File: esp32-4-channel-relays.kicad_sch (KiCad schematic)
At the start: 5 parts, among them U1 AMS1117-3.3

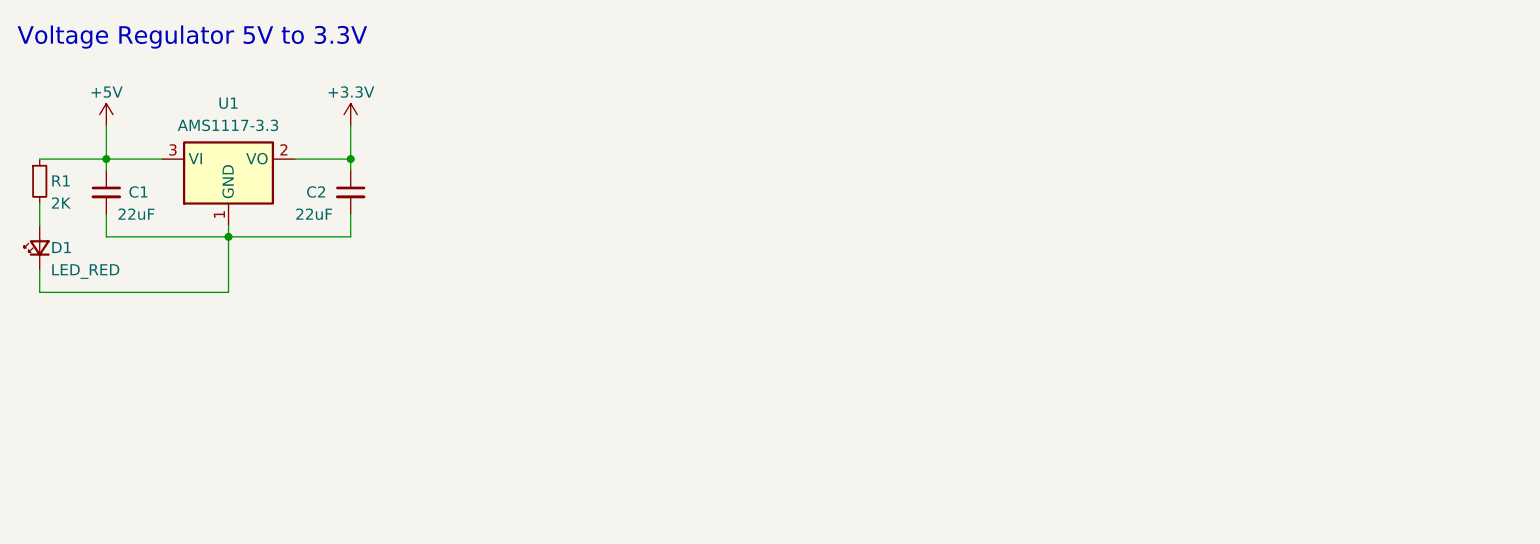
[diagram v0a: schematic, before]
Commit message: Add USB to serial converter
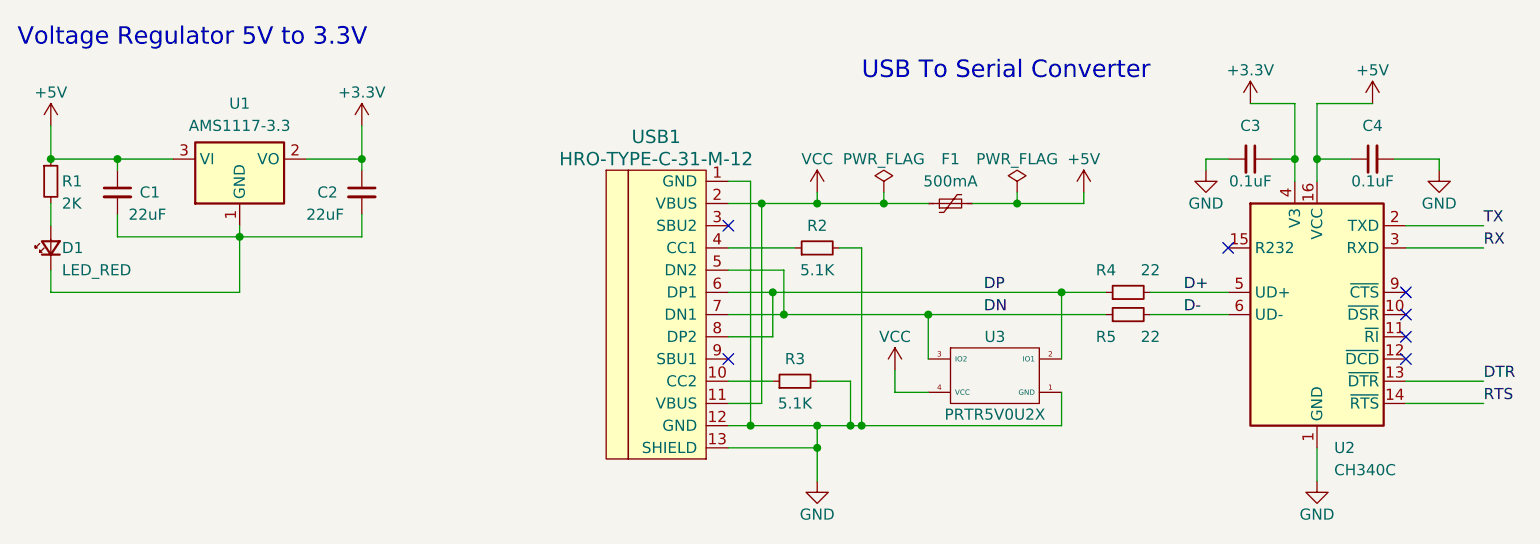
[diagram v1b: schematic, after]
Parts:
- added C3, C4: 0.1uF, symbol Device:C_Small
- added F1: 500mA, symbol Device:Polyfuse_Small
- added R2, R3: 5.1K, symbol Device:R_Small
- added R4, R5: 22, symbol Device:R_Small
- added U2: CH340C, Package_SO:SOIC-16_3.9x9.9mm_P1.27mm, symbol local_lib:CH340C
- added U3: PRTR5V0U2X, Package_TO_SOT_SMD:SOT-143, symbol local_lib:PRTR5V0U2X
- added USB1: HRO-TYPE-C-31-M-12, symbol local_lib:HRO-TYPE-C-31-M-12
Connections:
- net +3.3V: now also C3.1, U2.4 (V3)
- net +5V: now also C4.1, F1.2, U2.16 (VCC)
- new net: R3.1, USB1.10 (CC2)
- new net: R2.1, USB1.4 (CC1)
- new net D+: R4.2, U2.5 (UD+)
- new net D-: R5.2, U2.6 (UD-)
- new net DN: R5.1, U3.3 (IO2), USB1.5 (DN2), USB1.7 (DN1)
- new net DP: R4.1, U3.2 (IO1), USB1.6 (DP1), USB1.8 (DP2)
- new net DTR: U2.13 (~{DTR})
- new net GND: C3.2, C4.2, R2.2, R3.2, U2.1 (GND), U3.1 (GND), USB1.1 (GND), USB1.12 (GND), USB1.13 (SHIELD)
- new net RTS: U2.14 (~{RTS})
- new net RX: U2.3 (RXD)
- new net TX: U2.2 (TXD)
- new net VCC: F1.1, U3.4 (VCC), USB1.11 (VBUS), USB1.2 (VBUS)
- no-connect marks 0 -> 7
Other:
- note added: "USB To Serial Converter"
- moved on the sheet: C1, C2, D1, R1, U1

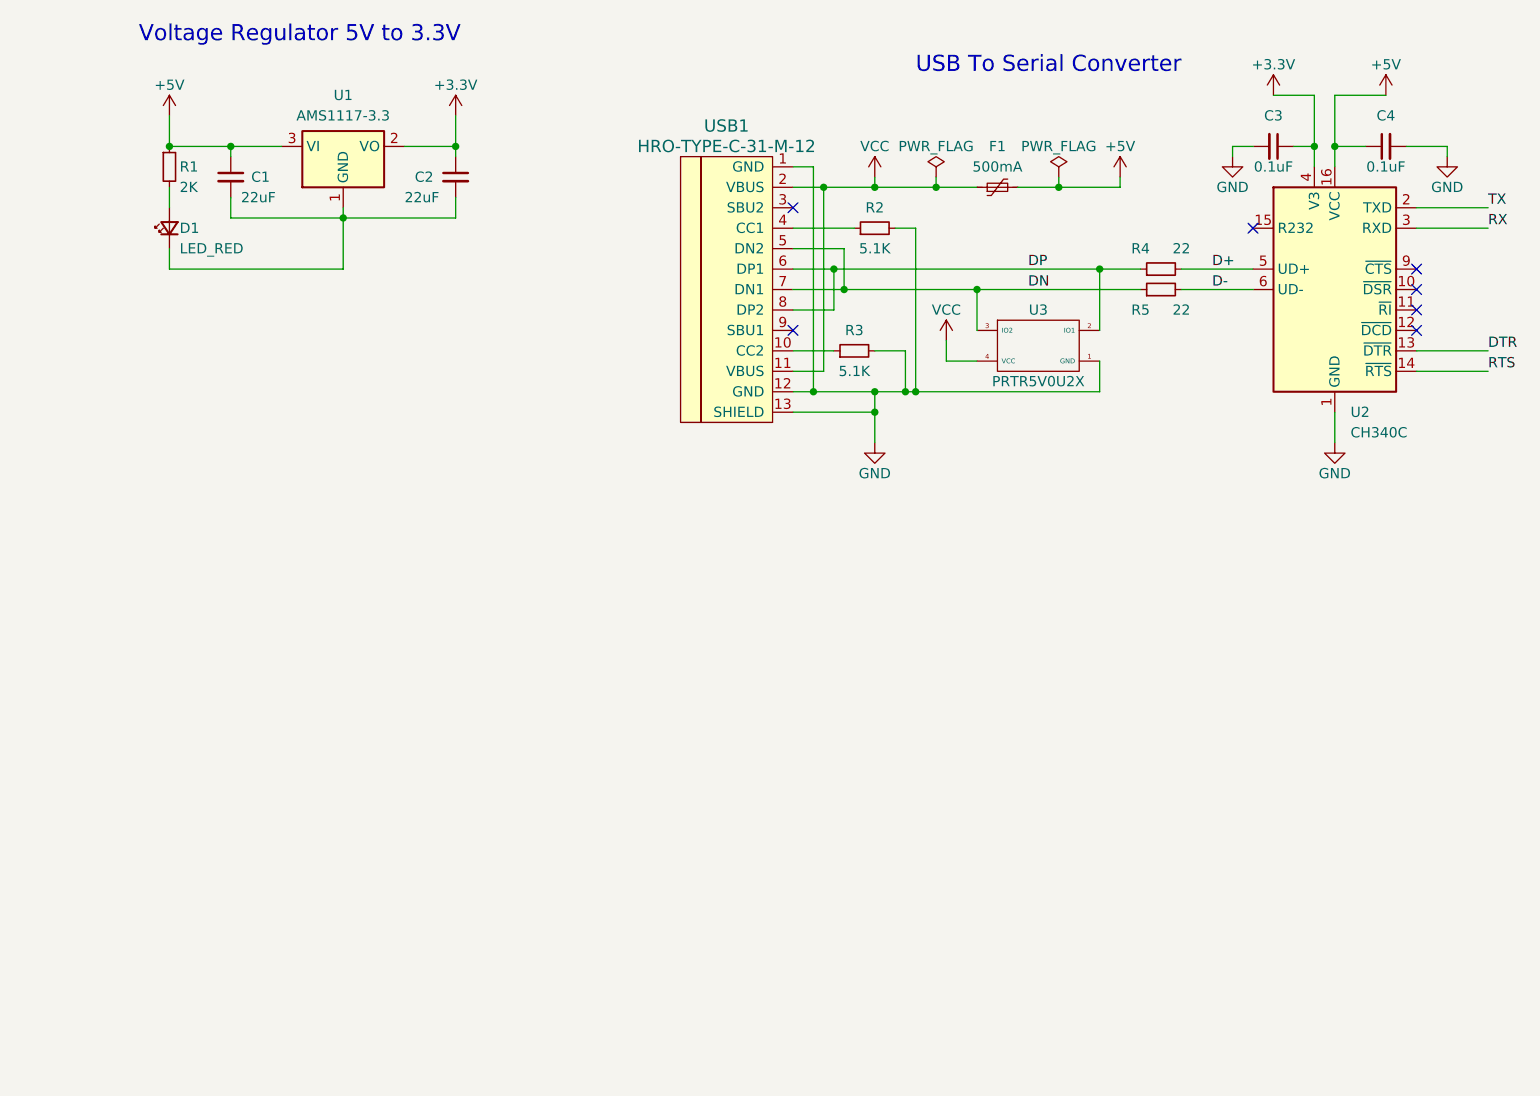
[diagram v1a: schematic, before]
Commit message: Add auto-reset
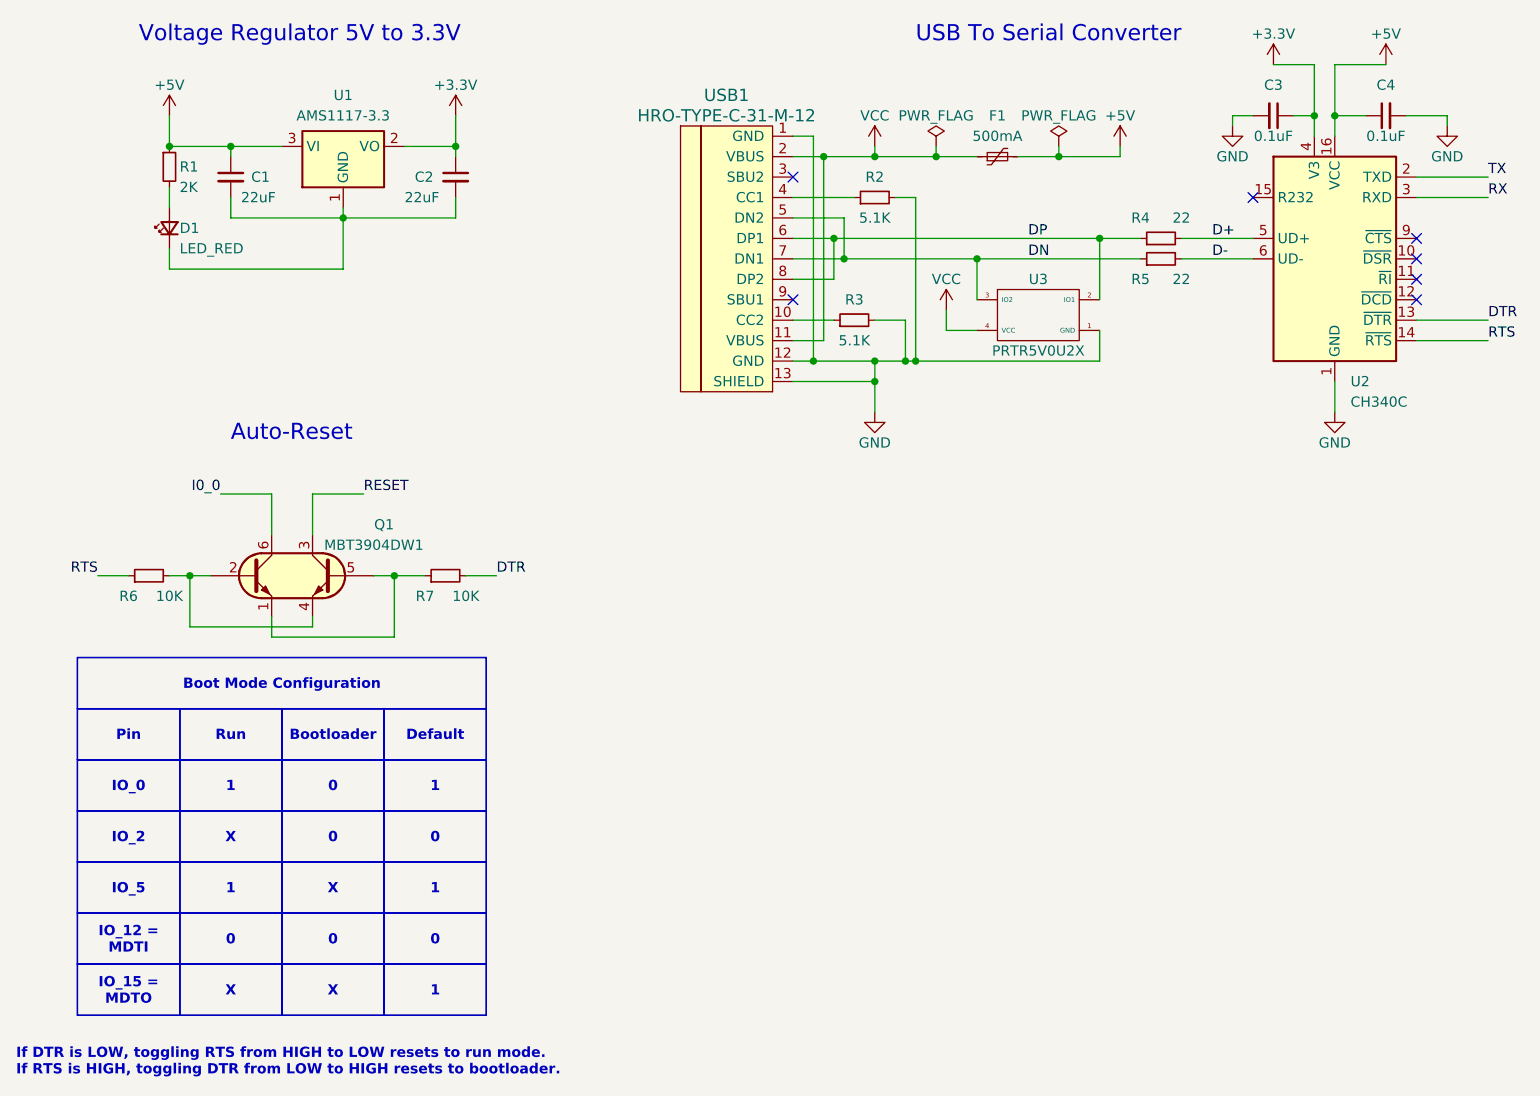
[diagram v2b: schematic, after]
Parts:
- added Q1: MBT3904DW1, Package_TO_SOT_SMD_AKL:SOT-363_SC-70-6, symbol local_lib:MBT3904DW1
- added R6, R7: 10K, symbol Device:R_Small
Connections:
- net DTR: now also R7.2
- net RTS: now also R6.1
- new net: Q1.1 (E1), Q1.5 (B2), R7.1
- new net: Q1.2 (B1), Q1.4 (E2), R6.2
- new net I0_0: Q1.6 (C1)
- new net RESET: Q1.3 (C2)
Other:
- note added: "Auto-Reset"
- note added: "If DTR is LOW, toggling RTS from HIGH to LOW resets to run mode. If RTS is HIGH, toggling DTR from LOW to HIGH resets to bootloader."
- moved on the sheet: C3, C4, F1, R2, R3, R4, R5, U2, U3, USB1

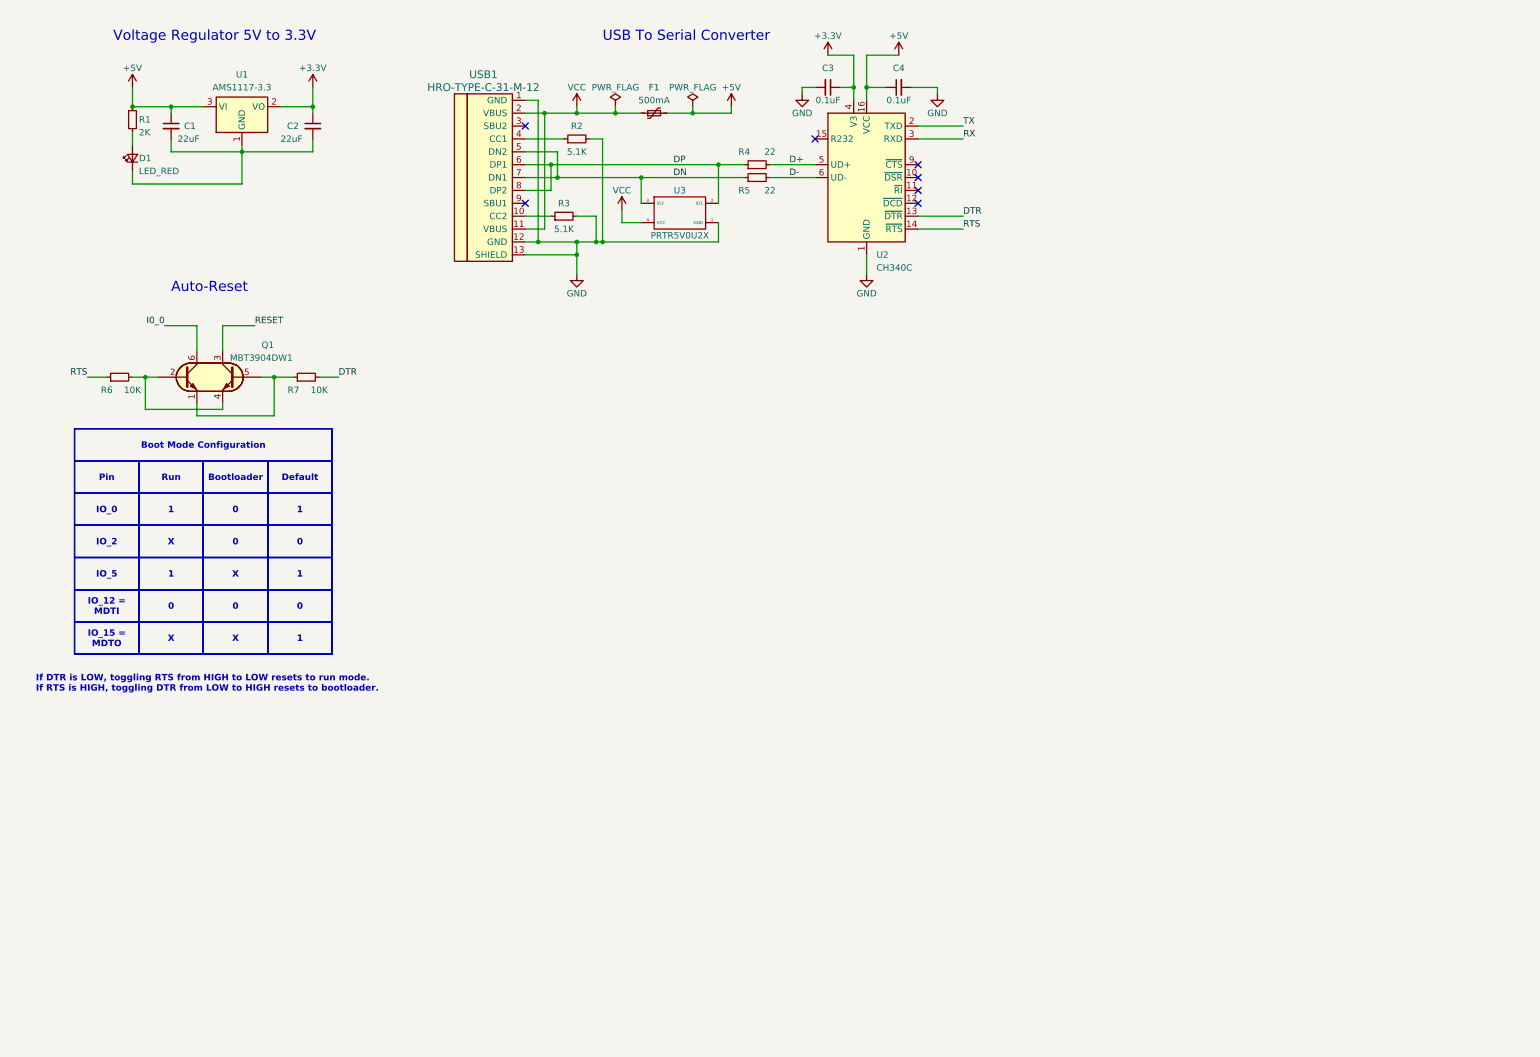
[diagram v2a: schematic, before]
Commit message: Add ESP32-WROOM-32 and reset button and boot button
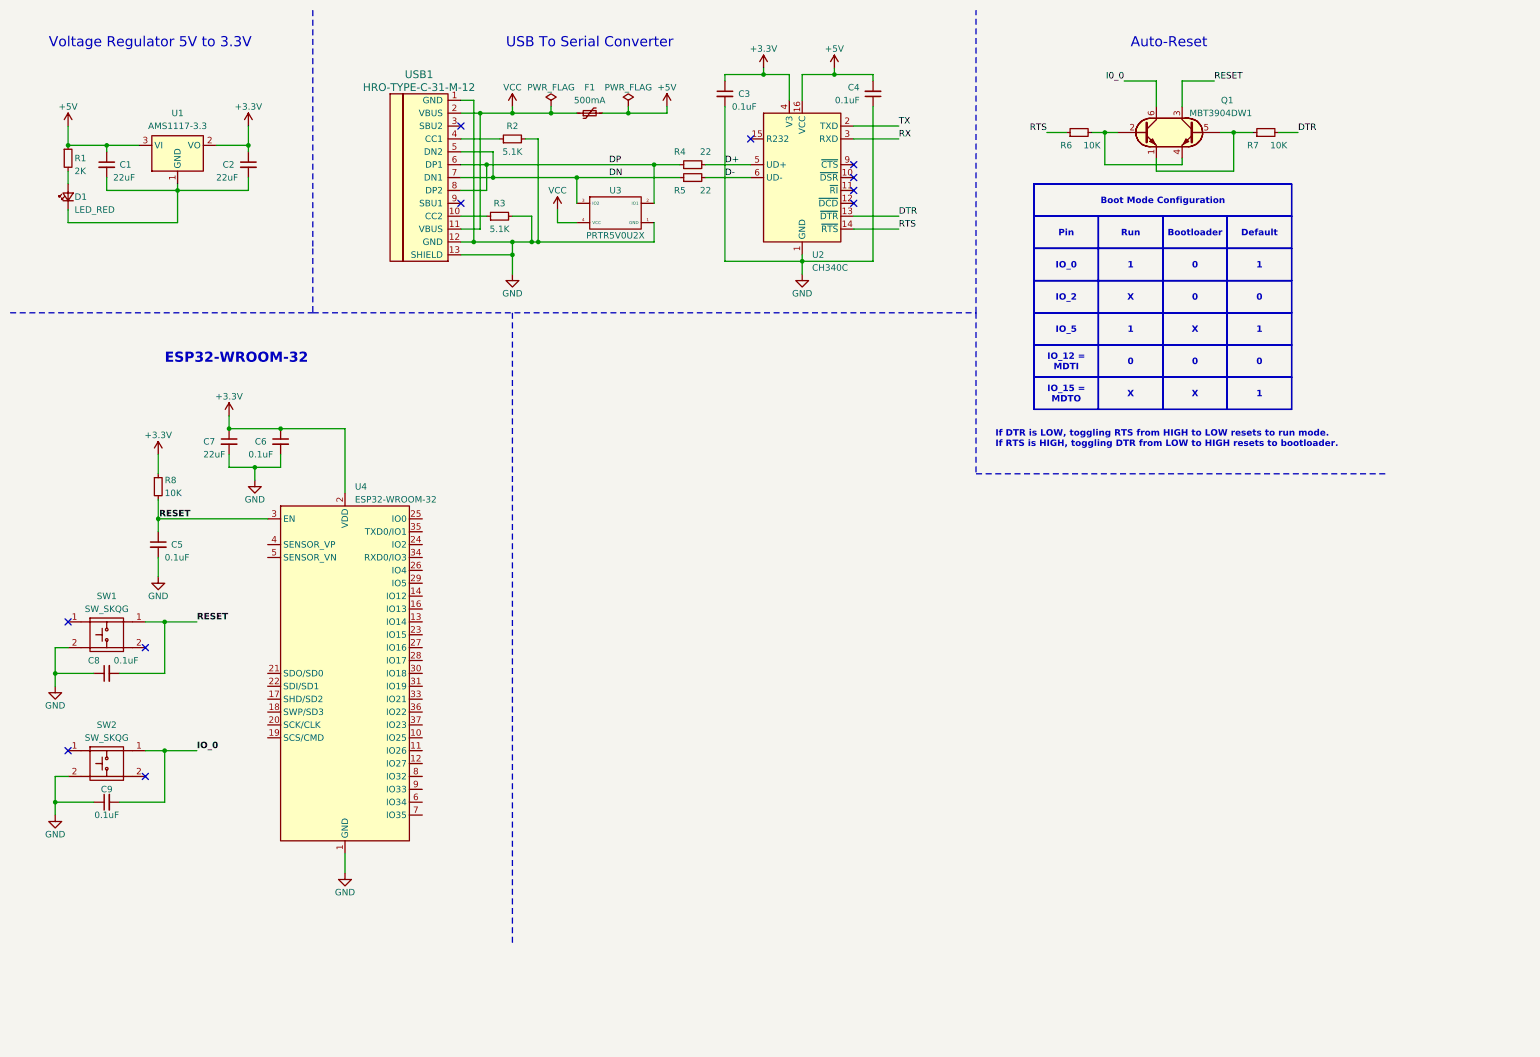
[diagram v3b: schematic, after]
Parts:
- added C5, C6, C8, C9: 0.1uF, symbol Device:C_Small
- added C7: 22uF, symbol Device:C_Small
- added R8: 10K, symbol Device:R_Small
- added SW1, SW2: SW_SKQG, Button_Switch_SMD:SW_SPST_SKQG_WithStem, symbol local_lib:SW_SKQG
- added U4: ESP32-WROOM-32, RF_Module:ESP32-WROOM-32, symbol local_lib:ESP32-WROOM-32
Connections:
- net D+ is gone; now on net GND: R4.2, U2.5 (UD+)
- net D- is gone; now on net GND: R5.2, U2.6 (UD-)
- net +3.3V: now also C6.1, C7.1, R8.1, U4.2 (VDD)
- net +5V: now also C4.2; no longer C4.1
- net GND: now also C4.1, C5.2, C6.2, C7.2, C8.1, C9.1, SW1.2, SW2.2, U4.1 (GND), U4.15 (GND), U4.38 (GND), U4.39 (GND); no longer C4.2
- net RESET: now also C5.1, C8.2, R8.2, SW1.1, U4.3 (EN)
- new net IO_0: C9.2, SW2.1
- no-connect marks 7 -> 11
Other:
- note added: "ESP32-WROOM-32"
- moved on the sheet: C1, C2, C3, C4, D1, F1, Q1, R1, R2, R3, R4, R5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
